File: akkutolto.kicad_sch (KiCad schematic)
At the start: 11 parts, among them U1 LM7805_TO220, U2 LM7805_TO220

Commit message: Pot_fix
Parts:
- RV2: value 470 -> 100
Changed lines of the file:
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@@
 			)
 		)
-		(property "Value" "470"
+		(property "Value" "100"
 			(at 144.78 77.47 90)
 			(effects

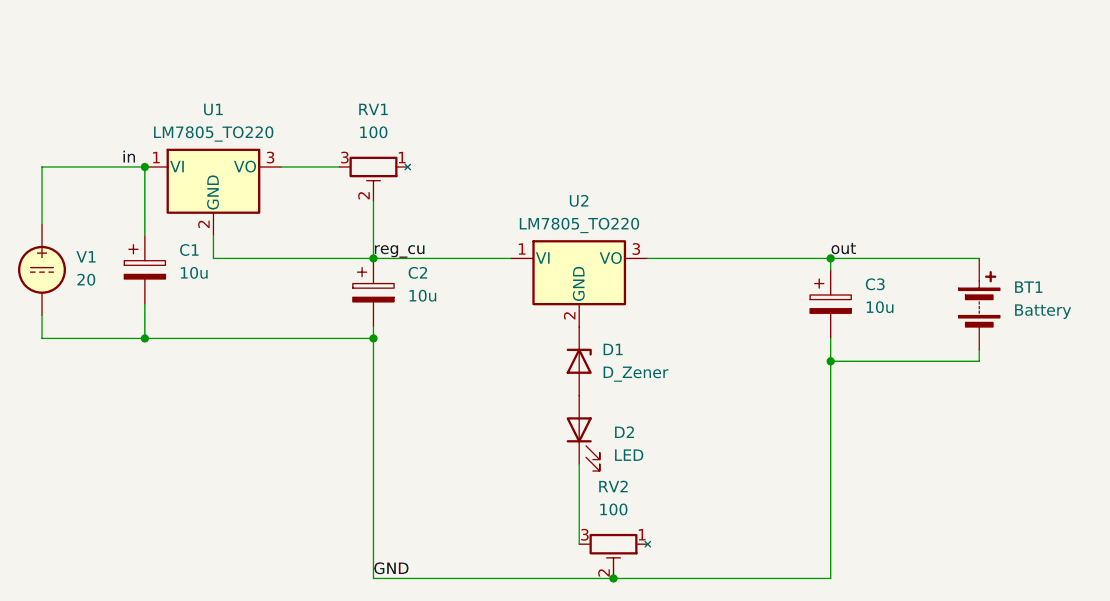
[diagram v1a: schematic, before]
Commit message: changed stabilizer to LM317
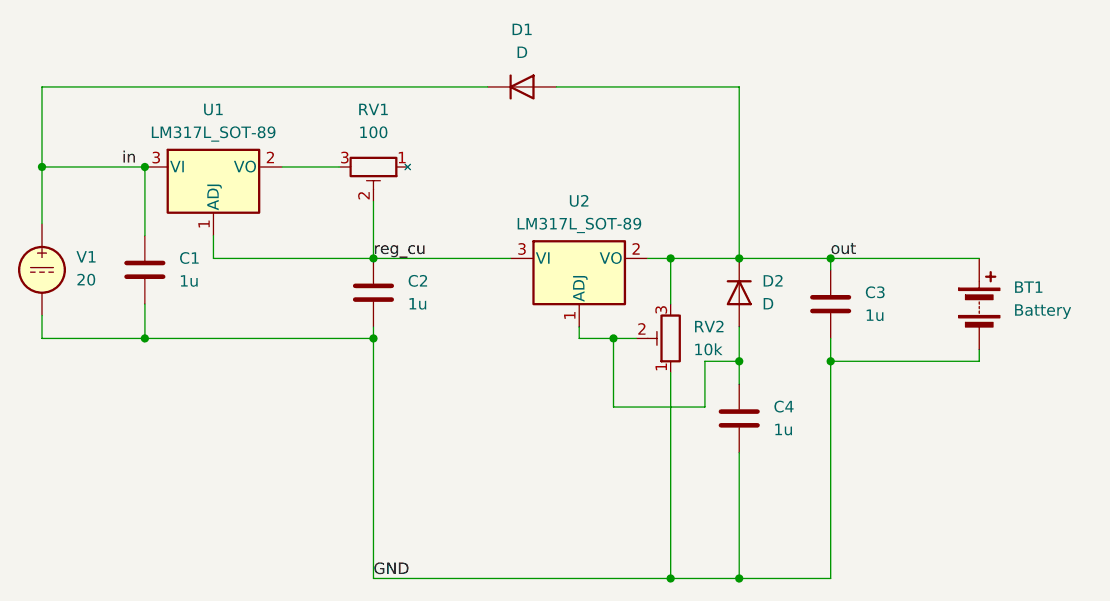
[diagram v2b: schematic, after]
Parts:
- removed C1, C2, C3: 10u, Capacitor_THT:CP_Radial_D6.3mm_P2.50mm, symbol Device:C_Polarized
- removed D1: D_Zener, Diode_THT:D_DO-41_SOD81_P7.62mm_Horizontal, symbol Device:D_Zener
- removed D2: LED, LED_SMD:LED_0805_2012Metric_Pad1.15x1.40mm_HandSolder, symbol Device:LED
- removed U1, U2: LM7805_TO220, Package_TO_SOT_THT:TO-220F-3_Horizontal_TabDown, symbol Regulator_Linear:LM7805_TO220
- added C1, C2, C3, C4: 1u, Capacitor_SMD:C_0805_2012Metric_Pad1.18x1.45mm_HandSolder, symbol Device:C
- added D1, D2: D, Diode_SMD:D_SOD-323_HandSoldering, symbol Device:D
- added U1, U2: LM317L_SOT-89, Package_TO_SOT_SMD:SOT-89-3, symbol Regulator_Linear:LM317L_SOT-89
- BT1: footprint (none) -> Connector_AMASS:AMASS_XT60-M_1x02_P7.20mm_Vertical
- RV2: value 100 -> 10k
- V1: footprint (none) -> Connector_BarrelJack:BarrelJack_Wuerth_6941xx301002
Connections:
- net GND: now also RV2.1, C1.2, C2.2, C3.2, C4.2; no longer RV2.2
- net in: now also C1.1, D1.1 (K), U1.3 (VI)
- net out: now also RV2.3, C3.1, D1.2 (A), D2.1 (K), U2.2 (VO)
- net reg_cu: now also C2.1, U1.1 (ADJ), U2.3 (VI)
- net at RV1.3: now also U1.2 (VO)
- new net: C4.1, D2.2 (A), RV2.2, U2.1 (ADJ)

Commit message: huzzad Pali
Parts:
- removed RV1: 100, Potentiometer_THT:Potentiometer_Runtron_RM-065_Vertical, symbol Device:R_Potentiometer_Trim
- removed U1, U2: LM317L_SOT-89, Package_TO_SOT_SMD:SOT-89-3, symbol Regulator_Linear:LM317L_SOT-89
- added R1: R, Resistor_THT:R_Axial_Power_L25.0mm_W9.0mm_P27.94mm, symbol Device:R
- added R2: R, Resistor_SMD:R_0805_2012Metric_Pad1.20x1.40mm_HandSolder, symbol Device:R
- added U1, U2: LM317_TO-220, Package_TO_SOT_THT:TO-220-3_Horizontal_TabDown, symbol Regulator_Linear:LM317_TO-220
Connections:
- net in: now also U1.3 (VI)
- net out: now also R2.1, U2.2 (VO); no longer RV2.3
- net reg_cu: now also R1.2, U1.1 (ADJ), U2.3 (VI)
- net at C4.1, D2.2 (A), RV2.2: now also R2.2, U2.1 (ADJ)
- new net: R1.1, U1.2 (VO)
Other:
- moved on the sheet: C1, C2, D1, V1
